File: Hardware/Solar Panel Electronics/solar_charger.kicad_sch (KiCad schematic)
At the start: 21 parts, among them J1 Screw_Terminal_SolarPanel_Inp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, J2 Screw_Terminal_Battery, U3 LT3652EDD

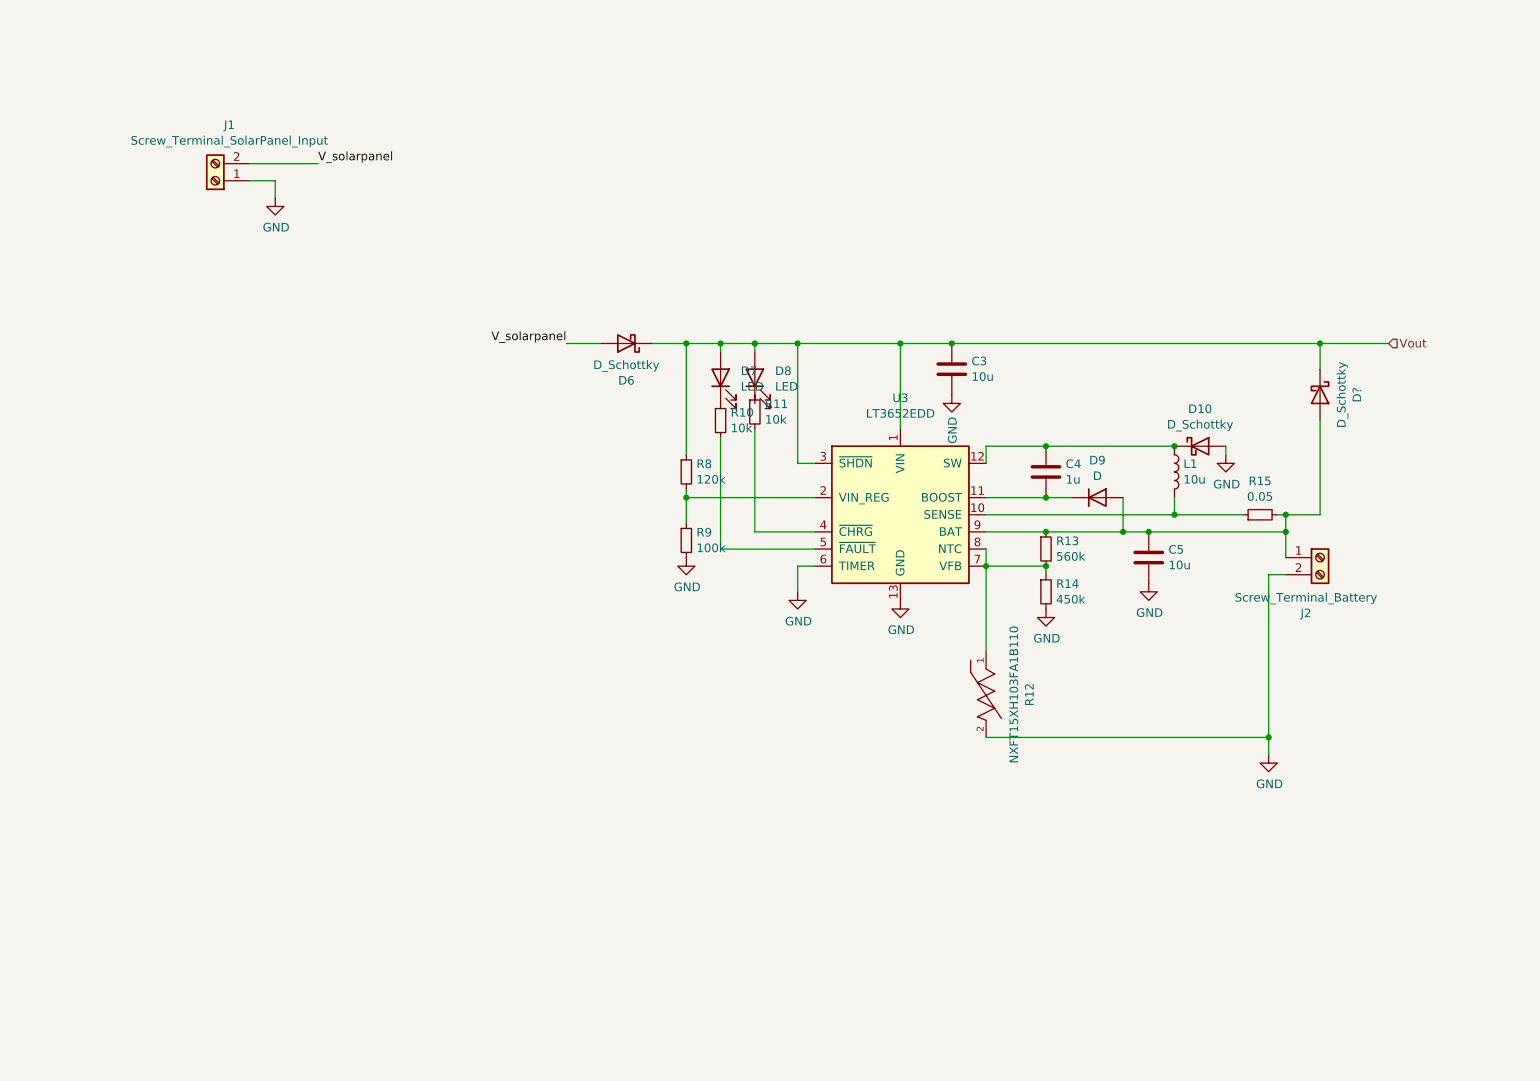
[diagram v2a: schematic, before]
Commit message: Components sized for our requirements. Added ideal diode IC LTC4411 which is more efficient than a normal diode.
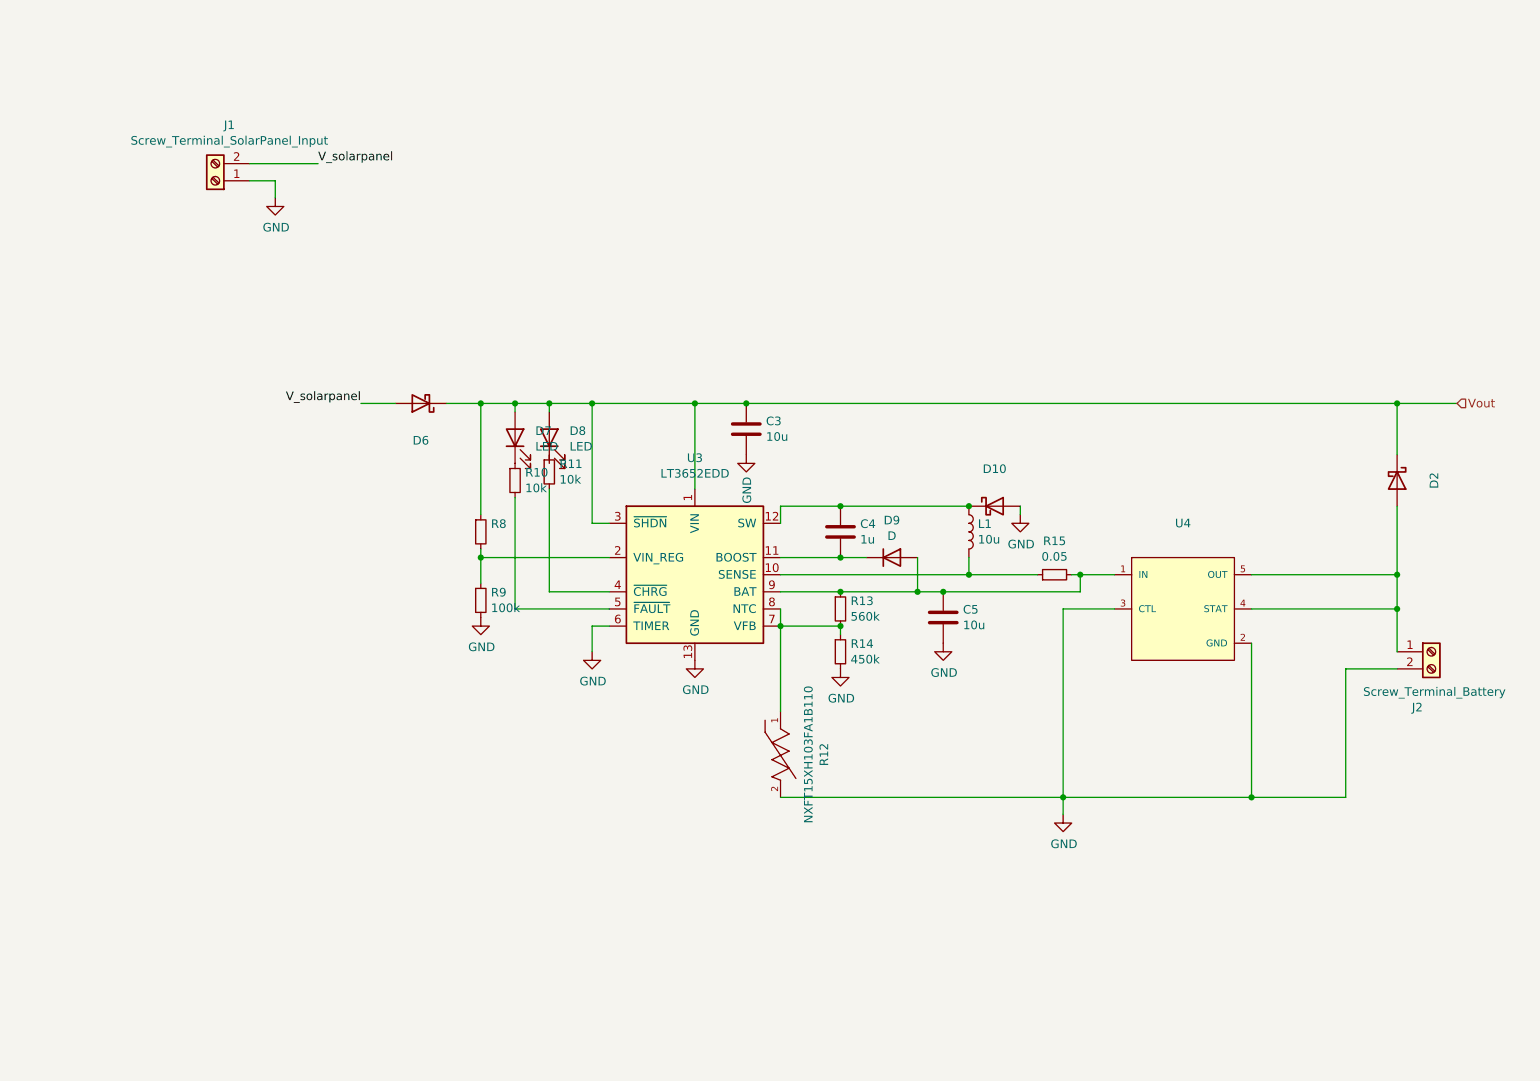
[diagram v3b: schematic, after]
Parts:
- added U4: (no value), symbol eec:LTC4411ES5TRMPBF
- D10, D6: value D_Schottky -> (none)
- D2: renamed from D?; value D_Schottky -> (none)
- R8: value 120k -> (none)
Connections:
- net GND: now also U4.2 (GND), U4.3 (CTL)
- net at C5.2, D9.2 (A), R13.1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: now also U4.1 (IN); no longer D2.2 (A), J2.1 (Pin_1)
- new net: D2.2 (A), J2.1 (Pin_1), U4.4 (STAT), U4.5 (OUT)
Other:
- moved on the sheet: C3, C4, C5, D10, D2, D6, D7, D8, D9, J2, L1, R10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

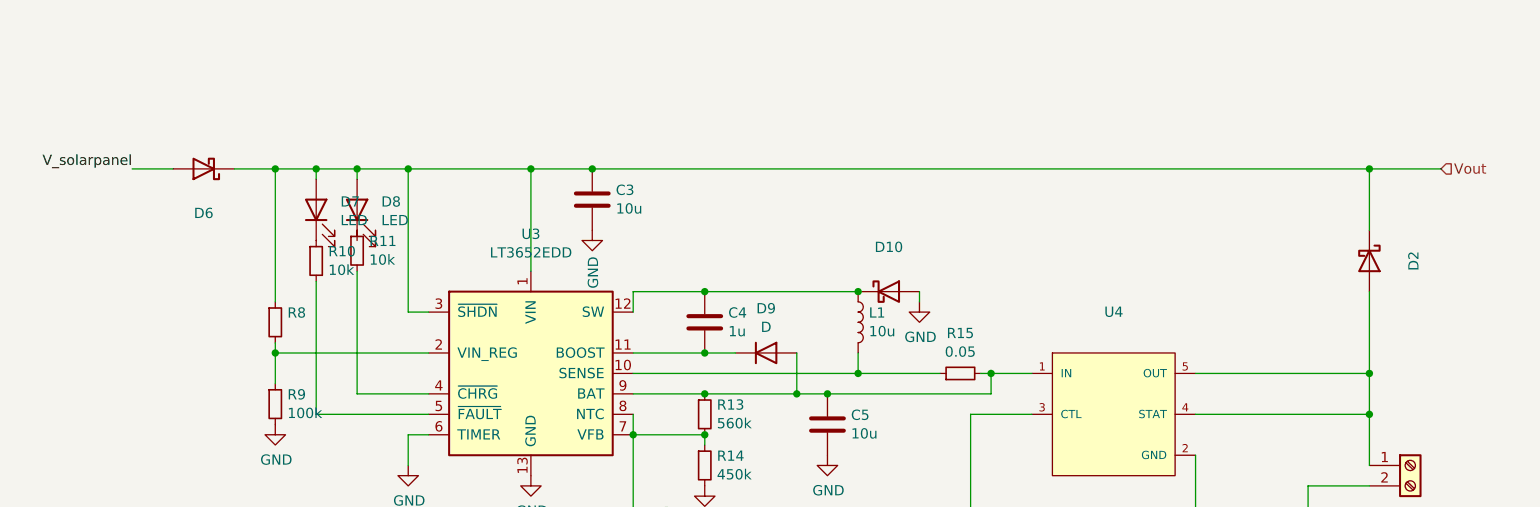
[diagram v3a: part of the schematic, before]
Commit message: Added voltage regulator from Pick Rick
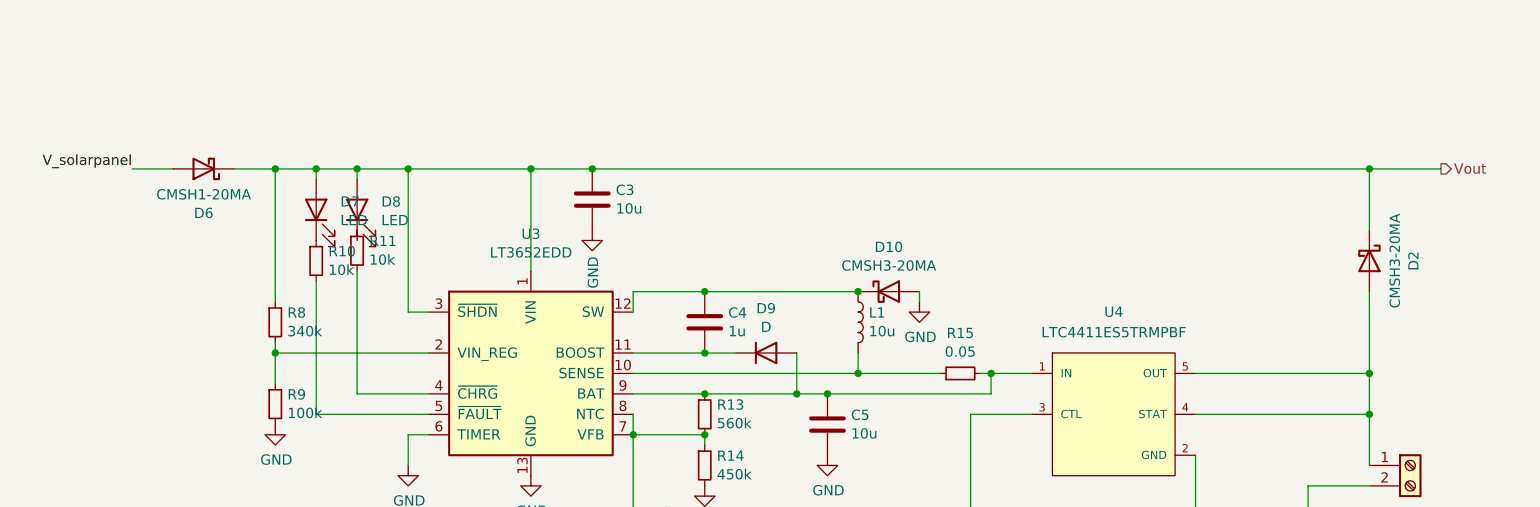
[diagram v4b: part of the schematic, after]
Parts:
- D10, D2: value (none) -> CMSH3-20MA
- D6: value (none) -> CMSH1-20MA
- R8: value (none) -> 340k
- U4: value (none) -> LTC4411ES5TRMPBF; footprint (none) -> Linear_Technology-LTC4411ES5TRMPBF-*
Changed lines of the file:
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@@
     (effects (font (size 1.27 1.27)) (justify right bottom))
   )
-  (hierarchical_label "Vout" (shape input) (at 228.6 72.39 0)
+  (hierarchical_label "Vout" (shape output) (at 228.6 72.39 0)
     (effects (font (size 1.27 1.27)) (justify left))
   )
@@
       (effects (font (size 1.27 1.27)) (justify left))
     )
-    (property "Value" "" (id 1) (at 85.3186 92.583 0)
+    (property "Value" "340k" (id 1) (at 85.3186 92.583 0)
       (effects (font (size 1.27 1.27)) (justify left))
     )
@@
     (in_bom yes) (on_board yes)
     (property "Reference" "D10" (id 0) (at 160.02 82.1182 0))
-    (property "Value" "" (id 1) (at 160.02 84.4296 0))
+    (property "Value" "CMSH3-20MA" (id 1) (at 160.02 84.4296 0))
     (property "Footprint" "" (id 2) (at 160.02 87.63 0)
       (effects (font (size 1.27 1.27)) hide)
@@
     (in_bom yes) (on_board yes)
     (property "Reference" "D6" (id 0) (at 74.93 77.9018 0))
-    (property "Value" "" (id 1) (at 74.93 75.5904 0))
+    (property "Value" "CMSH1-20MA" (id 1) (at 74.93 75.5904 0))
     (property "Footprint" "" (id 2) (at 74.93 72.39 0)
       (effects (font (size 1.27 1.27)) hide)
@@
     (in_bom yes) (on_board yes)
     (property "Reference" "D2" (id 0) (at 225.2218 83.82 0))
-    (property "Value" "" (id 1) (at 222.9104 83.82 0))
+    (property "Value" "CMSH3-20MA" (id 1) (at 222.9104 83.82 0))
     (property "Footprint" "" (id 2) (at 219.71 83.82 0)
       (effects (font (size 1.27 1.27)) hide)
@@
     (in_bom yes) (on_board yes) (fields_autoplaced)
     (property "Reference" "U4" (id 0) (at 187.96 90.17 0))
-    (property "Value" "" (id 1) (at 187.96 92.71 0))
-    (property "Footprint" "" (id 2) (at 175.26 87.63 0)
-      (effects (font (size 1.27 1.27)) (justify left) hide)
-    )
+    (property "Value" "LTC4411ES5TRMPBF" (id 1) (at 187.96 92.71 0))
+    (property "Footprint" "Linear_Technology-LTC4411ES5TRMPBF-*" (id 2) (at 175.26 87.63 0)
+      (effects (font (size 1.27 1.27)) (justify left) hide)
+    )

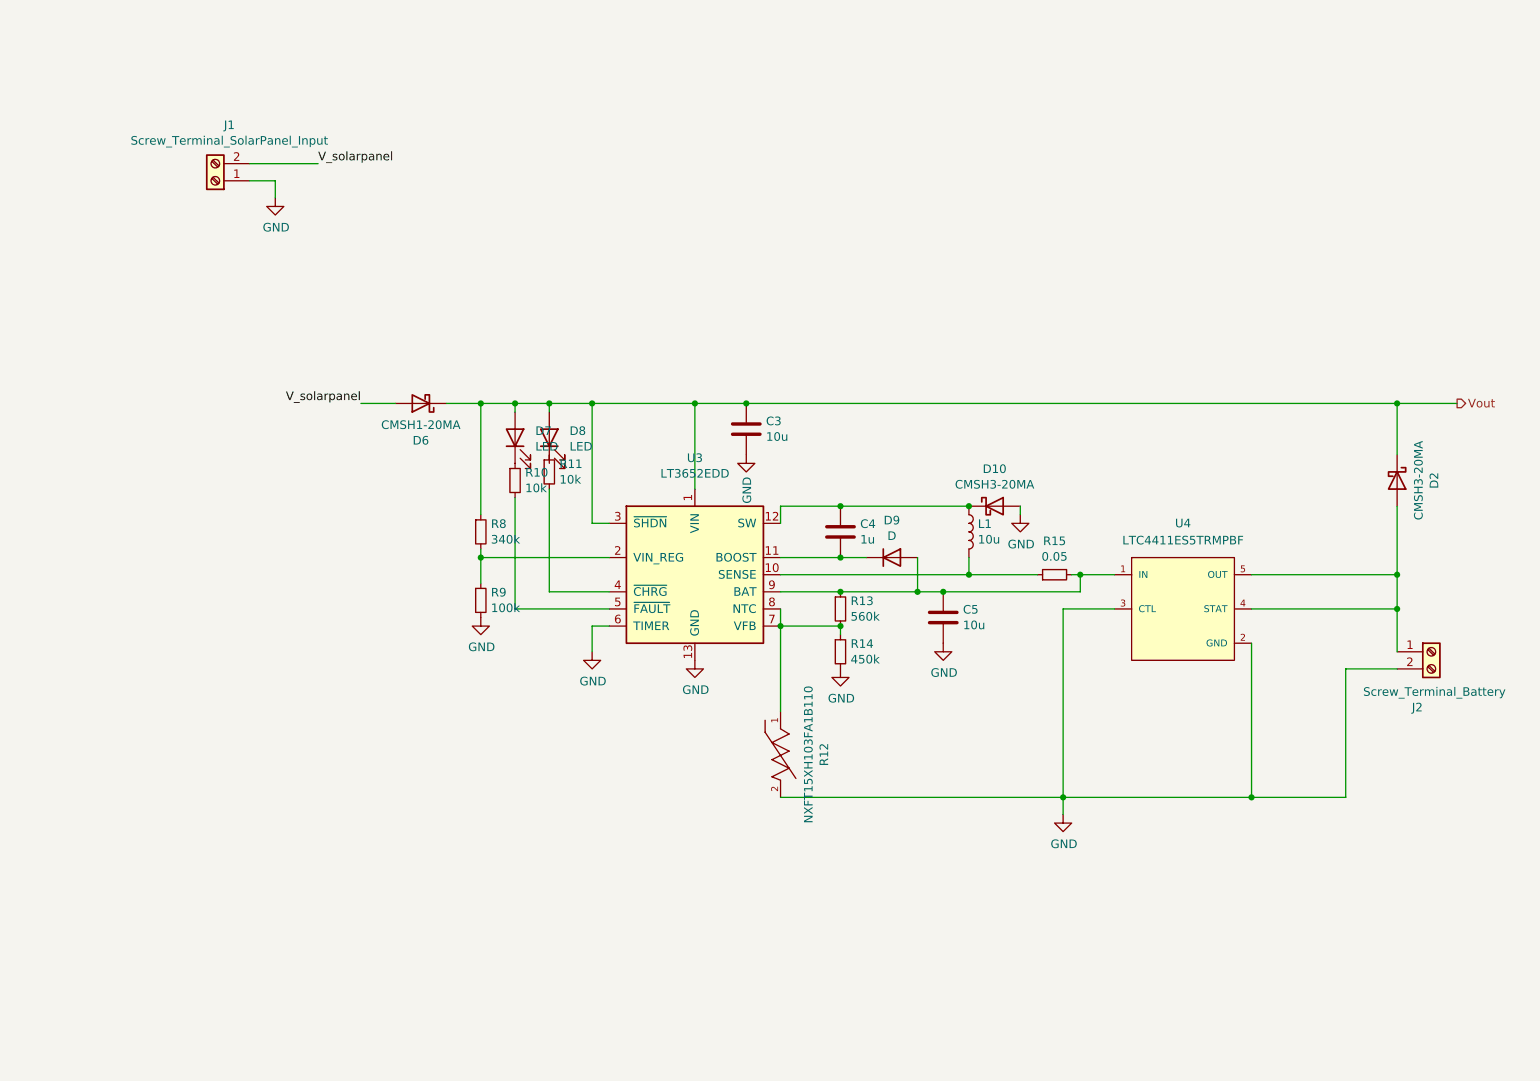
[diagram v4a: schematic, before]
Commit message: Made changes to solar charging circuit
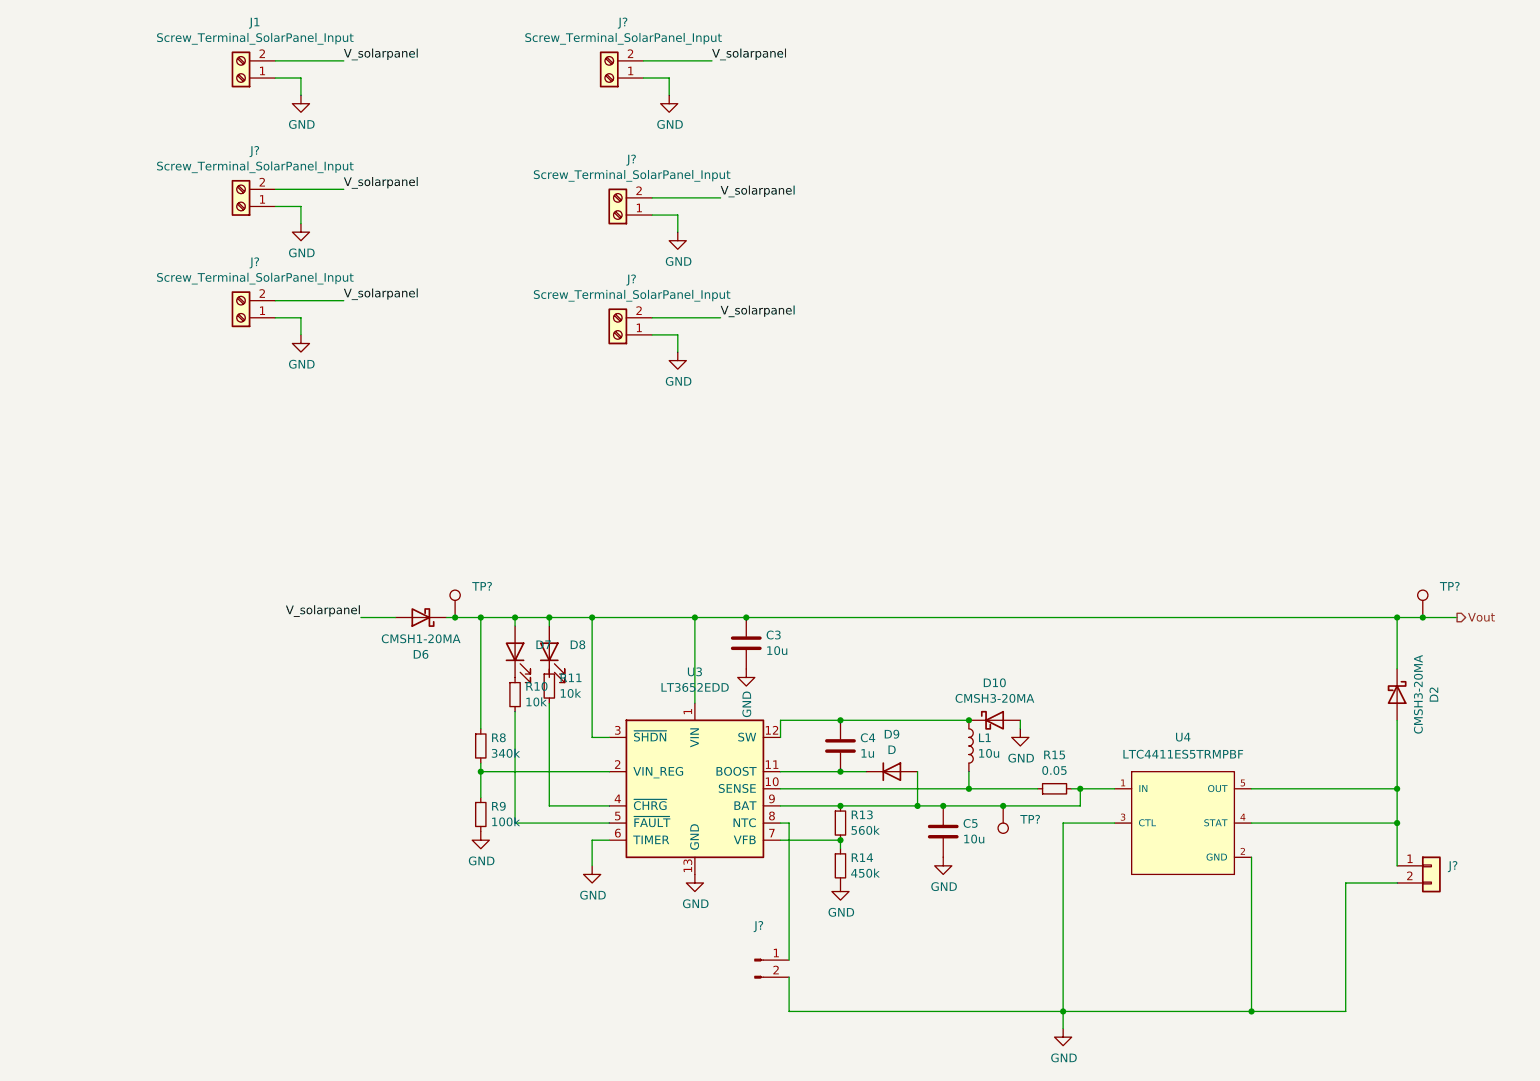
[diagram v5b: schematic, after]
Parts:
- removed J2: Screw_Terminal_Battery, symbol Connector:Screw_Terminal_01x02
- removed R12: NXFT15XH103FA1B110, Murata_Electronics_North_America-NXF_151B110-0-0-*, symbol solarpowerPCB-rescue:NXFT15XH103FA1B110-Thermistor
- added J? (x5): Screw_Terminal_SolarPanel_Input, symbol Connector:Screw_Terminal_01x02
- added J?: (no value), symbol Connector:Conn_01x02_Male
- added J?: (no value), symbol Connector_Generic:Conn_01x02
- added TP? (x3): (no value), symbol Connector:TestPoint
- D7, D8: value LED -> (none)
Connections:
- net GND: now also J?.1 (Pin_1), J?.1 (Pin_1), J?.1 (Pin_1), J?.1 (Pin_1), J?.1 (Pin_1), J?.2 (Pin_2), J?.2 (Pin_2)
- net V_solarpanel: now also J?.2 (Pin_2), J?.2 (Pin_2), J?.2 (Pin_2), J?.2 (Pin_2), J?.2 (Pin_2)
- net Vout: now also TP?.1, TP?.1
- net at R13.2, R14.1, U3.7 (VFB): no longer U3.8 (NTC)
- net at C5.2, D9.2 (A), R13.1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: now also TP?.1
- net at D2.2 (A), U4.4 (STAT), U4.5 (OUT): now also J?.1 (Pin_1)
- new net: J?.1 (Pin_1), U3.8 (NTC)
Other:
- moved on the sheet: C3, C4, C5, D10, D2, D6, D7, D8, D9, J1, L1, R10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
